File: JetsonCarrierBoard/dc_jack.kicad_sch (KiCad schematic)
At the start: 9 parts

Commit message: Adding more Title block info and changing main hierarchical page layout
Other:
- title: (none) -> 9-26V DC Jack
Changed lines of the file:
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@@
 (kicad_sch (version 20211123) (generator eeschema)
   (paper "A4")
+  (title_block
+    (title "9-26V DC Jack")
+    (date "2022-09-18")
+    (rev "1.0")
+  )
   (junction (at 123.19 93.98) (diameter 0) (color 0 0 0 0)
   )

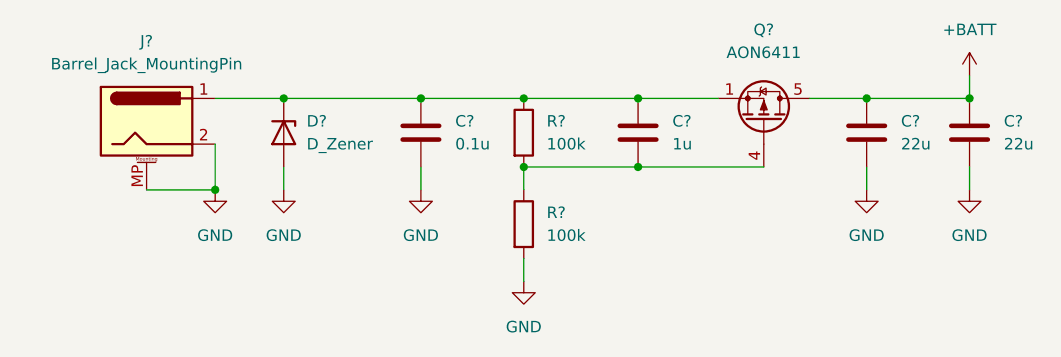
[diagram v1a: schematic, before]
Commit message: Improvement list, fixes, and readability improvements
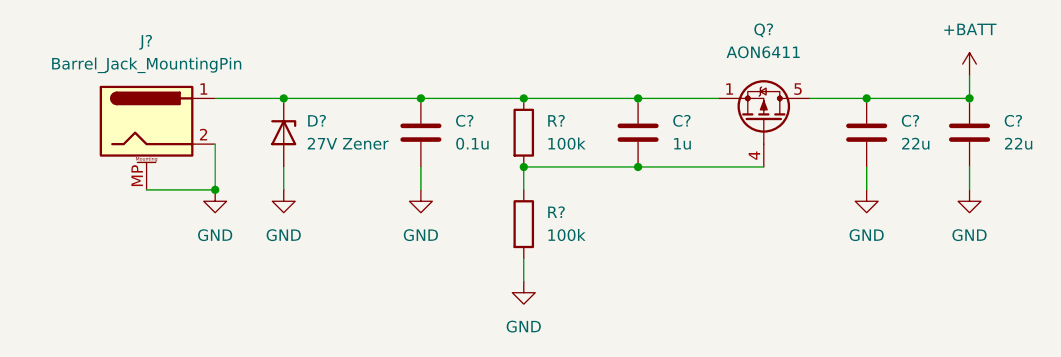
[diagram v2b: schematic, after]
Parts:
- D?: value D_Zener -> 27V Zener
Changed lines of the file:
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@@
       (effects (font (size 1.27 1.27)) (justify left))
     )
-    (property "Value" "D_Zener" (id 1) (at 125.73 99.0599 90)
+    (property "Value" "27V Zener" (id 1) (at 125.73 99.0599 90)
       (effects (font (size 1.27 1.27)) (justify left))
     )
